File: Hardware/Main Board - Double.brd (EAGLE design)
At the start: 124.5 x 73.7 mm, 114 parts, among them J1 MICROMOD-2222-C, J10 MICRO-SD-PUSH-PUSH-EXT-PIN, J2 Vertical Qwiic Connector, J4 QWIIC_RIGHT_ANGLE, J5 CORTEX_JTAG_DEBUG_MINIMUM_PTH, J6 MICROMOD_FUNCTION_MAIN, J7 MICROMOD_FUNCTION_MAIN, Q1 3.1A/30V/105mΩ, U1 STG3856QTR, U2 MCP73831, U5 AP7361C-33

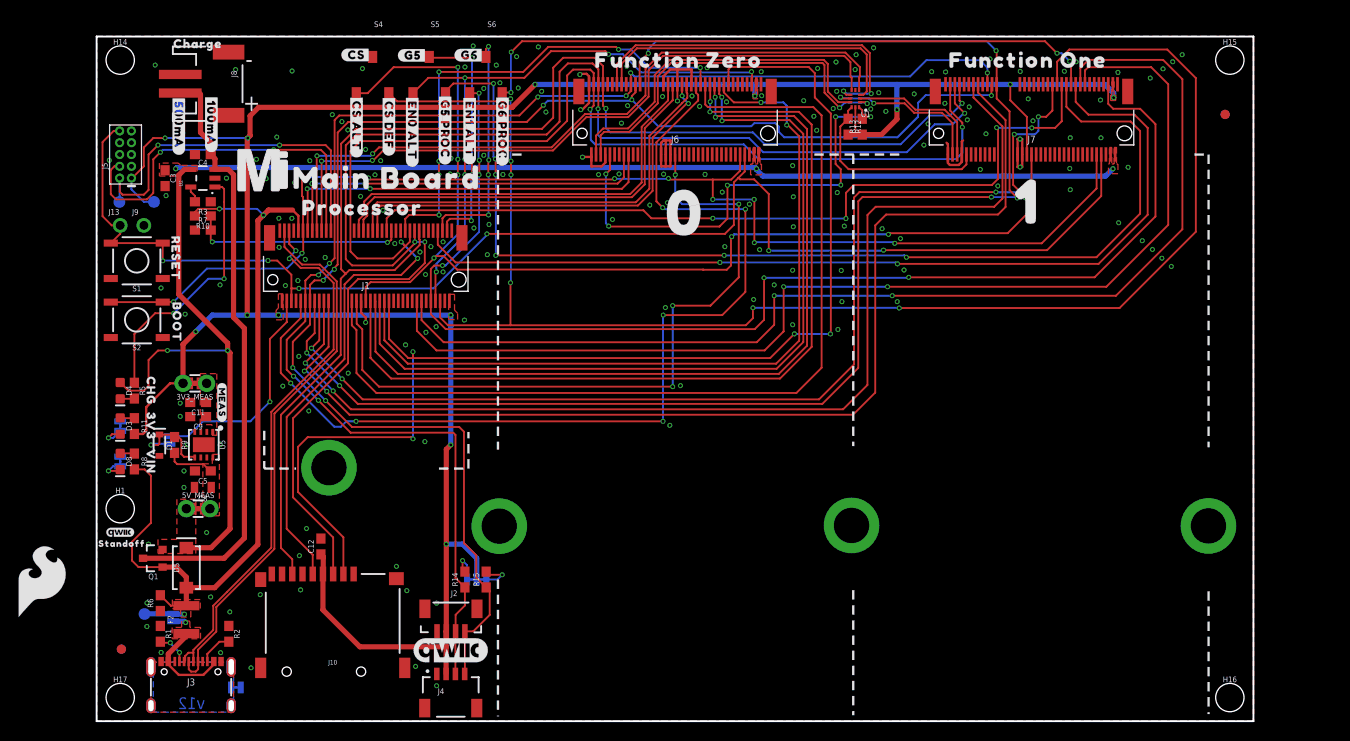
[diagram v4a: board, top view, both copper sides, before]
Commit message: Adds ESD protection to USB lines, replaces switches with cheaper more widely available ones
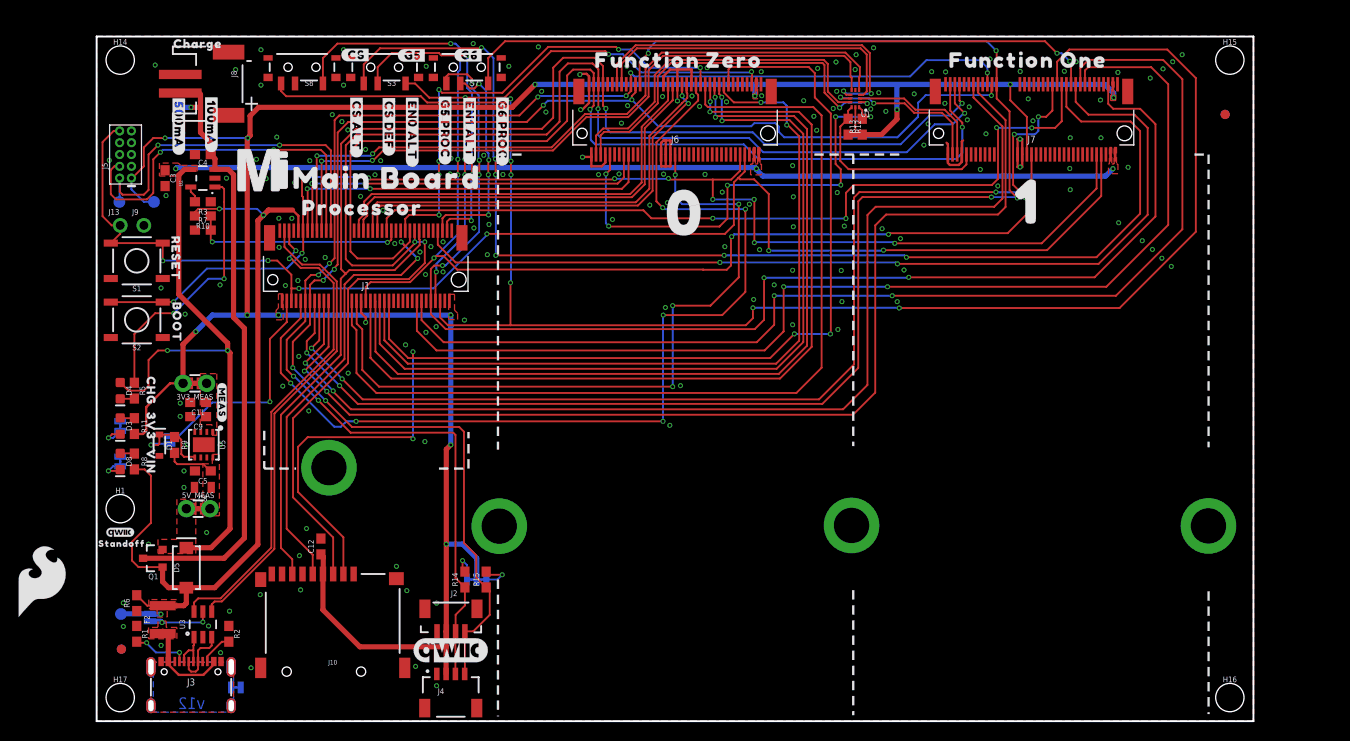
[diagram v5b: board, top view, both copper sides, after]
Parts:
- removed S4, S5, S6: DIPSWITCH-3-PIN, dip_switch:DIPSWITCH-SPDT
- added S3, S7, S8: (no value), SparkFun-Switches:SWITCH_SPST_SMD_A
- added U3: ESD Diode, SparkFun-DiscreteSemi:SOT-23-6
- moved BYP 2.54 mm to (5.71, 11.2)
- moved R1 2.54 mm to (4.32, 9.40)
- moved R6 2.54 mm to (4.32, 12.7)
- moved TP4 2.54 mm to (2.62, 11.5)
- moved F2 2.54 mm to (7.11, 10.9)
- moved U$3 2.54 mm to (8.59, 11.1)
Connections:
- new net N$7: J3.A6, J3.B6, U3.3
- new net N$8: J3.A7, J3.B7, U3.1
- net !CS1!-PROC-JUMPER: now also S8.2; no longer S4.P2
- net !CS1!-PROCESSOR: now also S8.1; no longer S4.P3
- net A1-PROCESSOR/!CS0!-ALT: now also S8.3; no longer S4.P1
- net D+: now also U3.4; no longer J3.A6, J3.B6
- net D-: now also U3.6; no longer J3.A7, J3.B7
- net G5-JUMPER: now also S3.2; no longer S5.P2
- net G5-PROCESSOR: now also S3.1; no longer S5.P3
- net G6-JUMPER: now also S7.2; no longer S6.P2
- net G6-PROCESSOR: now also S7.3; no longer S6.P3
- net GND: now also U3.2
- net SDIO_DATA1/PWR_EN1_ALT: now also S7.1; no longer S6.P1
- net SDIO_DATA2/PWR_EN0_ALT: now also S3.3; no longer S5.P1
- net V_USB: now also U3.5
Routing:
- net G5-PROCESSOR: track 116.0 -> 130.2 mm
- net !CS1!-PROCESSOR: track 162.0 -> 174.6 mm
- net D+: track 58.9 -> 50.5 mm
- net A1-PROCESSOR/!CS0!-ALT: track 119.2 -> 127.6 mm
- net G5-JUMPER: track 26.0 -> 34.0 mm
- net N$7: track 0.00 -> 7.14 mm
- net D-: track 58.1 -> 52.5 mm
- net V_USB: track 11.9 -> 17.4 mm, vias 1 -> 2
- net SDIO_DATA1/PWR_EN1_ALT: track 132.0 -> 136.7 mm
- net N$8: track 0.00 -> 4.57 mm
- net VIN: track 89.6 -> 92.3 mm
- net N$5: track 3.56 -> 6.10 mm
- net G6-JUMPER: track 25.9 -> 23.5 mm
- net V_BATT: track 64.6 -> 66.9 mm, vias 0 -> 1
- net !CS0!-PROCESSOR: track 52.4 -> 51.6 mm
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
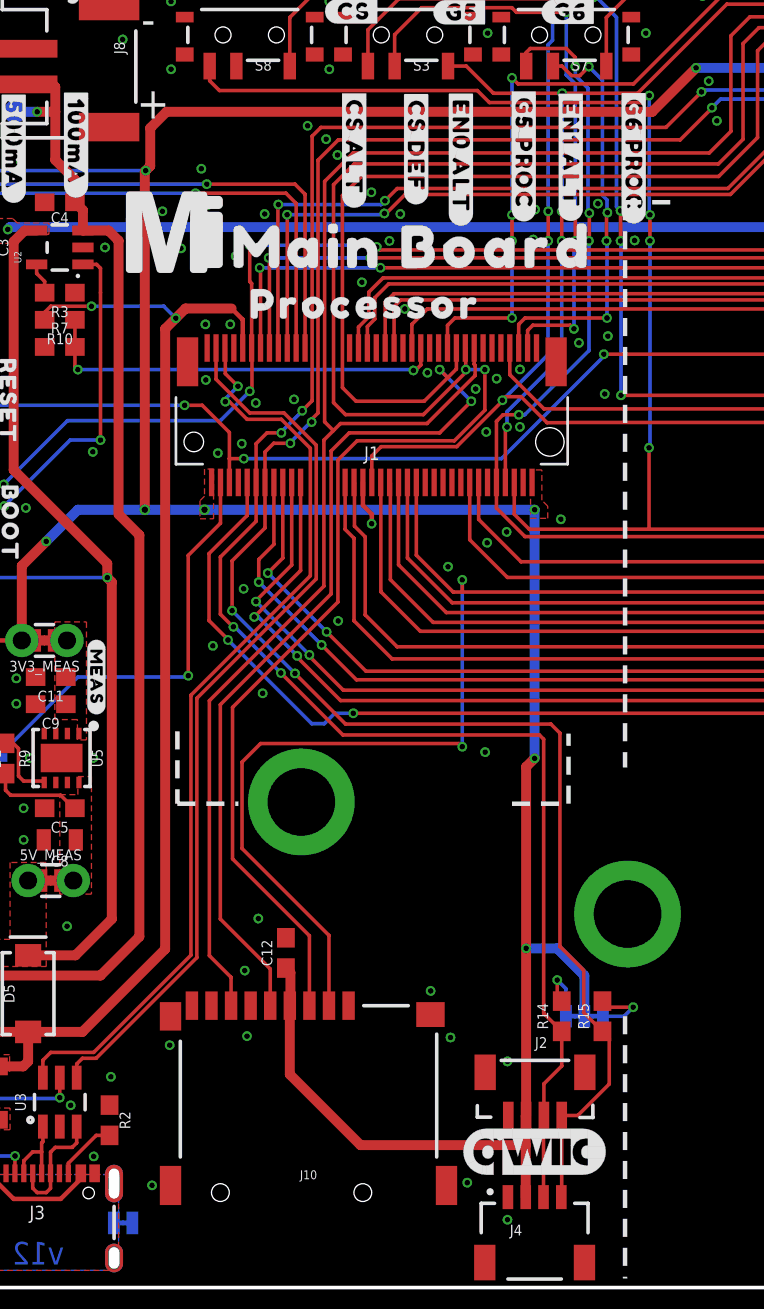
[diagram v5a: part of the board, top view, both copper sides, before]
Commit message: Adds new VREG, new VREG added to control 3.3V @ Qwiic Connectors, moves i2c pullup jumper (connected to 3v3 not 3v3_Qwiic)
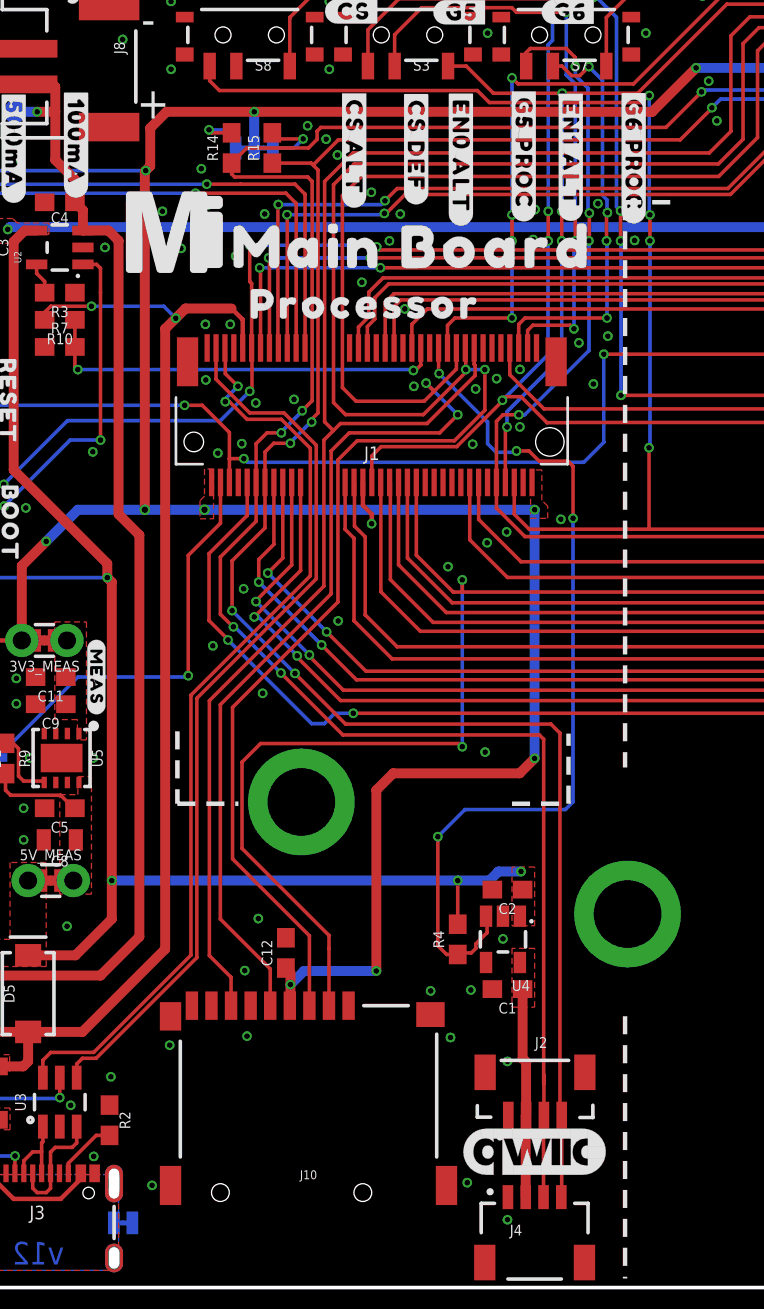
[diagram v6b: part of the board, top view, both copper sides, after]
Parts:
- added C1, C2: 1.0uF, SparkFun-Capacitors:0603
- added R4: 100k, SparkFun-Resistors:0603
- added U4: 3.3V, dip_switch:SOT25
- moved I2C_PU 52.2 mm to (22.4, 64.0)
- moved R14 52.2 mm to (21.1, 64.0)
- moved R15 52.2 mm to (23.4, 64.0)
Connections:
- removed net I2C_SCL1-PROCESSOR: J1.53
- removed net I2C_SDA1-PROCESSOR: J1.51
- new net 3.3V_QWIIC: C1.1, J2.2, J4.2, U4.5
- new net I2C_SCL1-PROCESSOR/QWIIC_EN: J1.53, R4.1, U4.3
- net 3.3V: no longer J2.2, J4.2
- net GND: now also C1.2, C2.2, U4.2
- net VCC: now also C2.1, R4.2, U4.1
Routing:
- net I2C_SCL1-PROCESSOR/QWIIC_EN: track 0.00 -> 49.9 mm, vias 0 -> 4
- net VCC: track 164.7 -> 190.3 mm, vias 5 -> 8
- net 3.3V: track 267.9 -> 245.1 mm, vias 13 -> 15
- net 3.3V_QWIIC: track 0.00 -> 11.8 mm
- net I2C_SDA: track 153.6 -> 161.5 mm
- net !RESET!: track 151.1 -> 154.1 mm
- net SPI_PROCESSOR_SCK: track 155.8 -> 154.7 mm
- net N$11: track 3.52 -> 4.10 mm
- net GND: vias 182 -> 184
- added copper zone on layer 1, net 3.3V_QWIIC

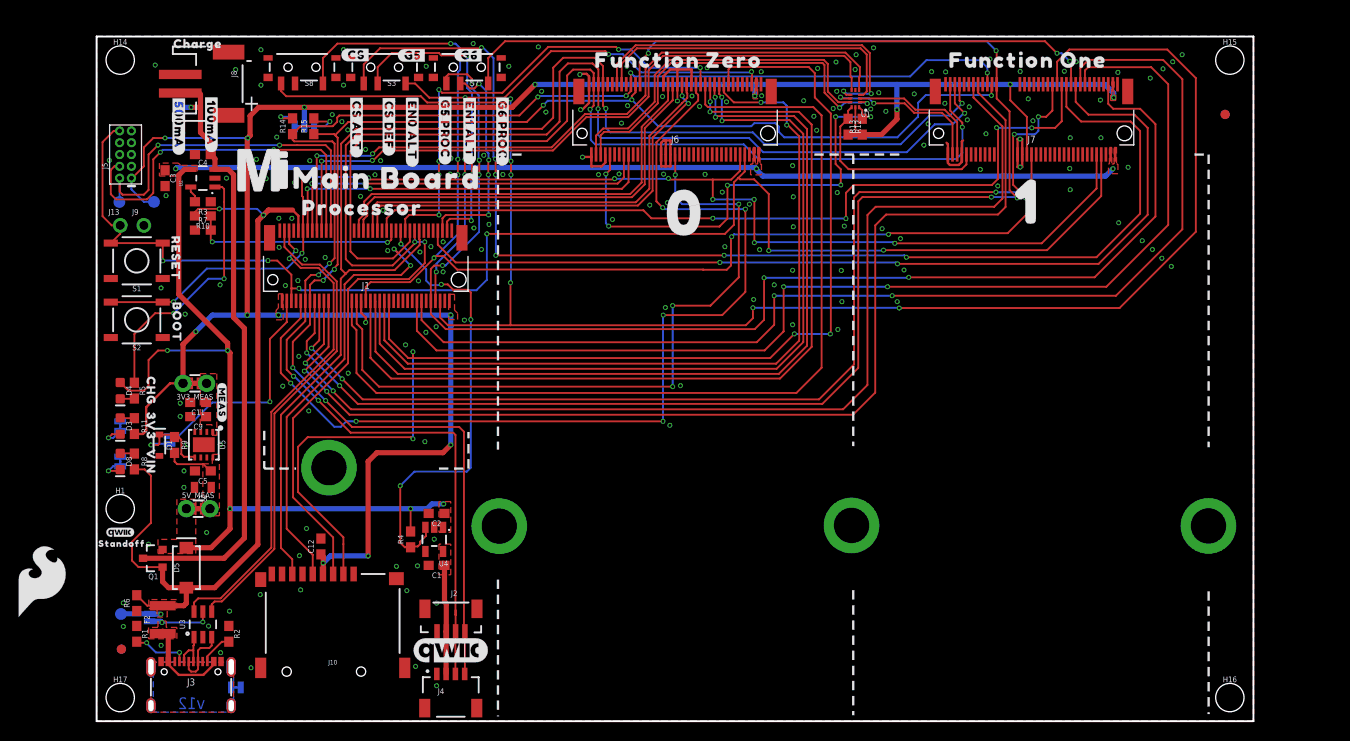
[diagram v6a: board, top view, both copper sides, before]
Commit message: Adds silk, updates alignment of existing silk that was not replaced, updates landing pads for new mux part
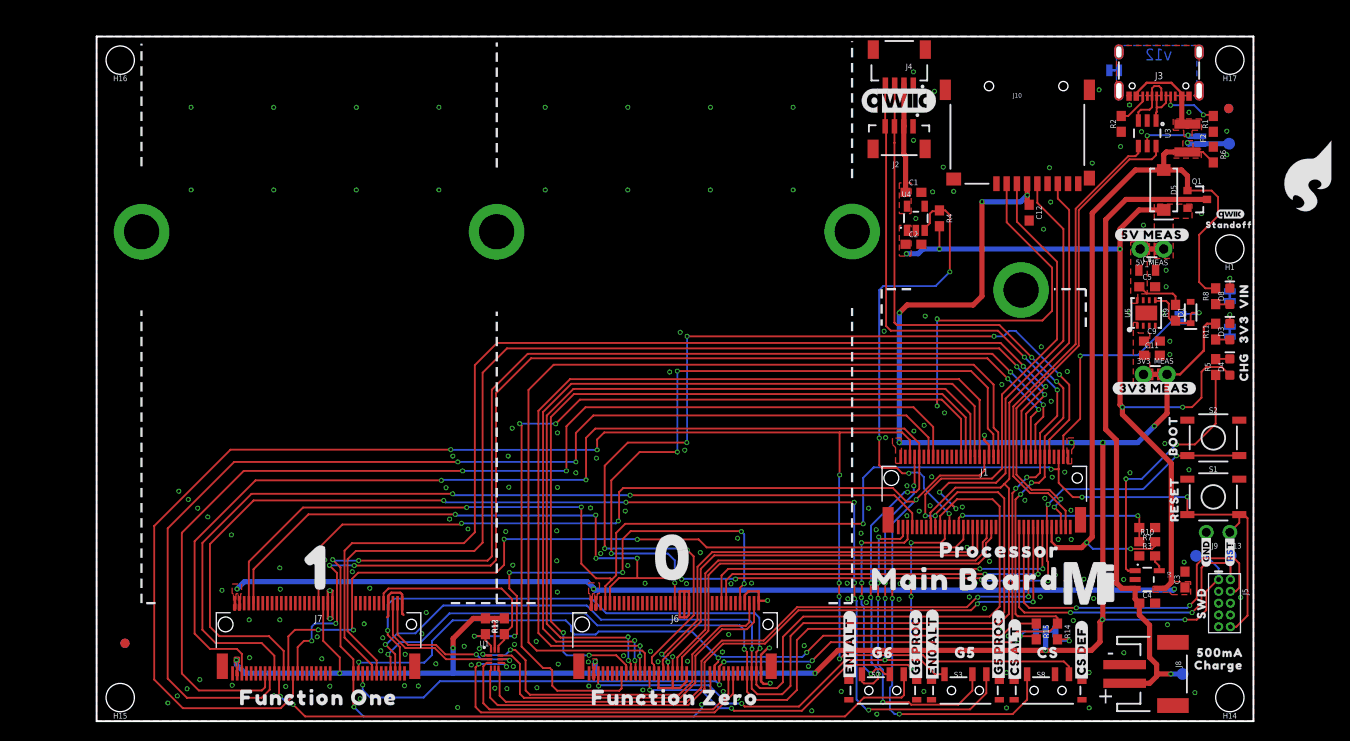
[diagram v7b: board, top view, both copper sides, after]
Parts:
- added U$31: (no value), top:#5V_MEAS#6522
- added U$39: (no value), top:#RST#6521
- added U$40: (no value), top:#GND#6520
- U$19: device top:#CS#18 -> top:G518
- U$25: device top:#500MA#21 -> top:SWD6522
- U$26: device top:#100MA#501 -> top:#3V3_MEAS#6522
- U$29: device top:#G5#18 -> top:G6519
- U$32: device top:#G6#18 -> top:CS17
- U$33: device top:#MEAS#40313513 -> top:500MA6520
- moved U$24 143.0 mm to (130.3, 58.7), turned to 180 degrees
- moved H14 137.7 mm to (121.9, 2.54), turned to 180 degrees
- moved H15 137.7 mm to (2.54, 2.54), turned to 180 degrees
- moved H16 137.7 mm to (2.54, 71.1), turned to 180 degrees
- moved H17 137.7 mm to (121.9, 71.1), turned to 180 degrees
- moved FD3 132.6 mm to (121.8, 65.9), turned to 270 degrees
- moved FD4 132.6 mm to (121.8, 65.9), turned to 90 degrees
- moved FD1 131.3 mm to (3.05, 8.38), turned to 180 degrees
- moved FD2 131.3 mm to (3.05, 8.38), turned to 180 degrees
- moved TP4 129.5 mm to (121.8, 62.1), turned to 180 degrees
- moved U$27 128.6 mm to (120.7, 6.02)
- moved R1 128.2 mm to (120.1, 64.3), turned to 90 degrees
- moved J5 127.7 mm to (121.3, 12.7), turned to 270 degrees
- moved TP1 125.5 mm to (122.0, 17.8), turned to 180 degrees
- moved R6 125.5 mm to (120.1, 61.0), turned to 270 degrees
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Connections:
- net A1-PROCESSOR/!CS0!-ALT renamed A1-PROCESSOR/!CS1!-ALT
- net RX1-AUX_TX-FC0-PLEX renamed RX1-DFU_TX-FC0-PLEX
- net RX1-AUX_TX-FC1-PLEX renamed RX1-DFU_TX-FC1-PLEX
- net TX1-AUX_RX-FC0-PLEX renamed TX1-DFU_RX-FC0-PLEX
- net TX1-AUX_RX-FC1-PLEX renamed TX1-DFU_RX-FC1-PLEX
- net G6-PROCESSOR: now also S7.1; no longer S7.3
- net SDIO_DATA1/PWR_EN1_ALT: now also S7.3; no longer S7.1
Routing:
- net G6-PROCESSOR: track 69.5 -> 73.7 mm
- net V_BATT: track 66.9 -> 70.6 mm
- net 3.3V: track 245.1 -> 246.9 mm
- net !RESET!: track 154.1 -> 155.3 mm
- net !DFU-FC0!: track 50.6 -> 51.8 mm
- net N$10: track 3.38 -> 2.26 mm
- net SDIO_DATA1/PWR_EN1_ALT: track 136.7 -> 135.6 mm
- net RX1-PROCESSOR-PLEX: track 39.1 -> 39.7 mm
- net G4-PROCESSOR/SD_CARD_!CS!: track 132.2 -> 131.6 mm
- net I2C_SCL: track 158.3 -> 157.8 mm
- net I2C_SDA: track 161.5 -> 161.0 mm

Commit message: Updates device name and removes value from new VREG
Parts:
- U4: value 3.3V -> AP7347DQ-33W5-7K-3.3V
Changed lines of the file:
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@@
 <attribute name="VALUE" x="110.49" y="63.246" size="0.6096" layer="27" font="vector" ratio="20" rot="R270" align="bottom-center"/>
 </element>
-<element name="U4" library="dip_switch" package="SOT25" value="3.3V" x="88.138" y="54.102" smashed="yes">
+<element name="U4" library="dip_switch" package="SOT25" value="AP7347DQ-33W5-7K-3.3V" x="88.138" y="54.102" smashed="yes">
 <attribute name="NAME" x="86.614" y="56.388" size="0.6096" layer="25" font="vector" ratio="20"/>
 <attribute name="PROD_ID" value="" x="88.138" y="54.102" size="1.778" layer="27" font="vector" ratio="15" display="off"/>
-<attribute name="VALUE" x="86.487" y="51.308" size="0.6096" layer="27" font="vector" ratio="20"/>
 </element>
 <element name="C1" library="SparkFun-Capacitors" package="0603" value="1.0uF" x="87.884" y="56.896" smashed="yes">
